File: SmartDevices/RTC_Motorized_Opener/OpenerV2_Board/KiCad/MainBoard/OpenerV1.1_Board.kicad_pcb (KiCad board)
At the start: 2 copper layers, 66 x 60 mm, 60 parts, among them IC1 CD4011BM96, J1 Motor, J2 Conn_01x02, J3 Conn_02x03_Odd_Even, J8 Conn_01x06, Q1 NPN, Q2 2N3904, Q3 AO3401A, Q4 AO3400A, Q5 2N3904, Q6 AO3400A, Q7 AO3401A, Q8 AO3400A, Q9 2N3904, SW1 Reset, SW2 Open, SW3 Menu, SW4 Close, U1 ATmega328P-AU, U2 MIC5205-5.0YM5, U3 DS1307, Y1 8/16MHz, Y2 32.768KHz

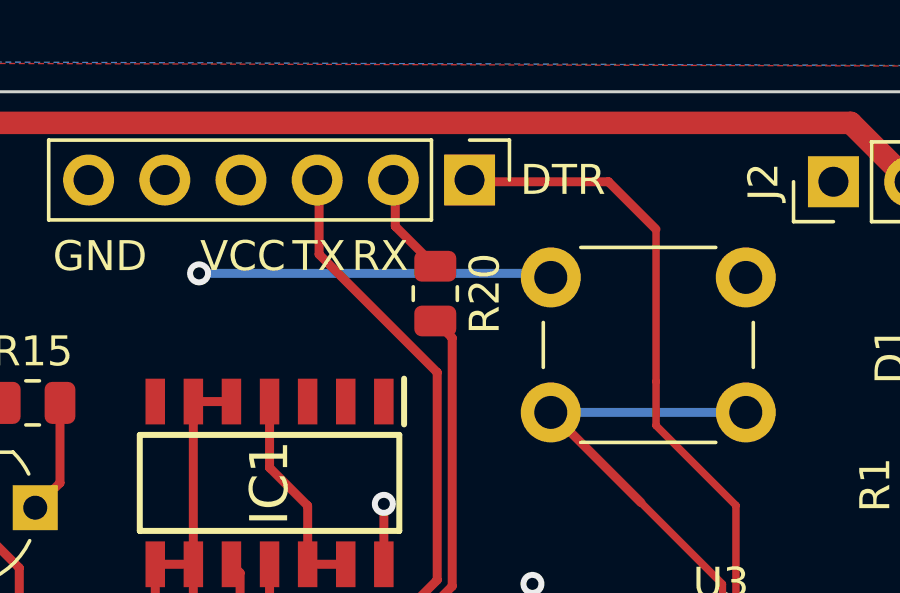
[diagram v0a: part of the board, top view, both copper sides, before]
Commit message: Fixed TX RX Swapped pins
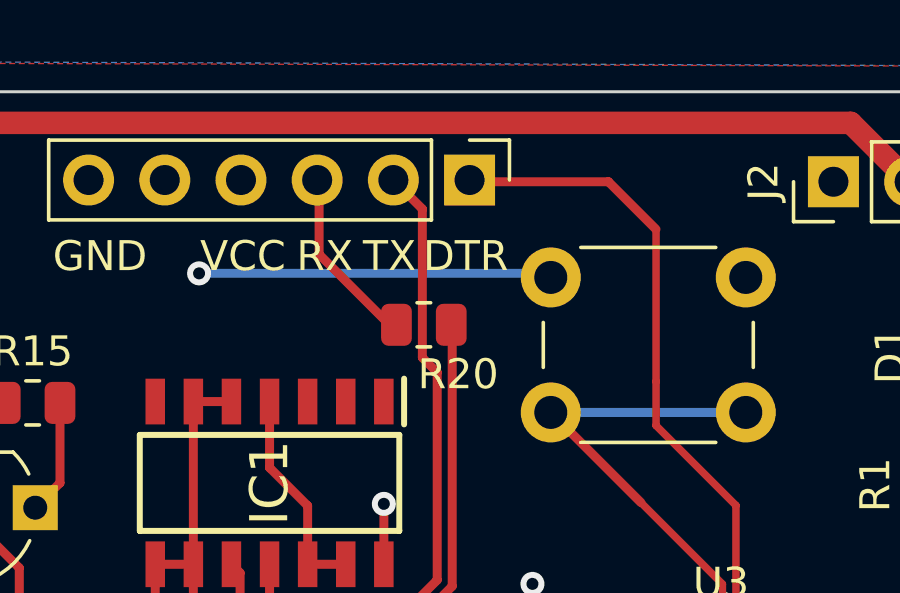
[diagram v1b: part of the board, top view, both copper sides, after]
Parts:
- moved R20 1.11 mm to (130.8, 48.8), turned to 0 degrees
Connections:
- J8 pad 2: Net-(J8-Pad2) -> Tx0
- J8 pad 3: Tx0 -> Net-(J8-Pad3)
- R20 pad 1: Net-(J8-Pad2) -> Net-(J8-Pad3)
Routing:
- net Net-(J8-Pad3): track 0.00 -> 5.97 mm
- net Net-(J8-Pad2): track 3.37 -> 0.00 mm
- net Tx0: track 38.6 -> 37.6 mm
- net Rx0: track 32.7 -> 31.9 mm

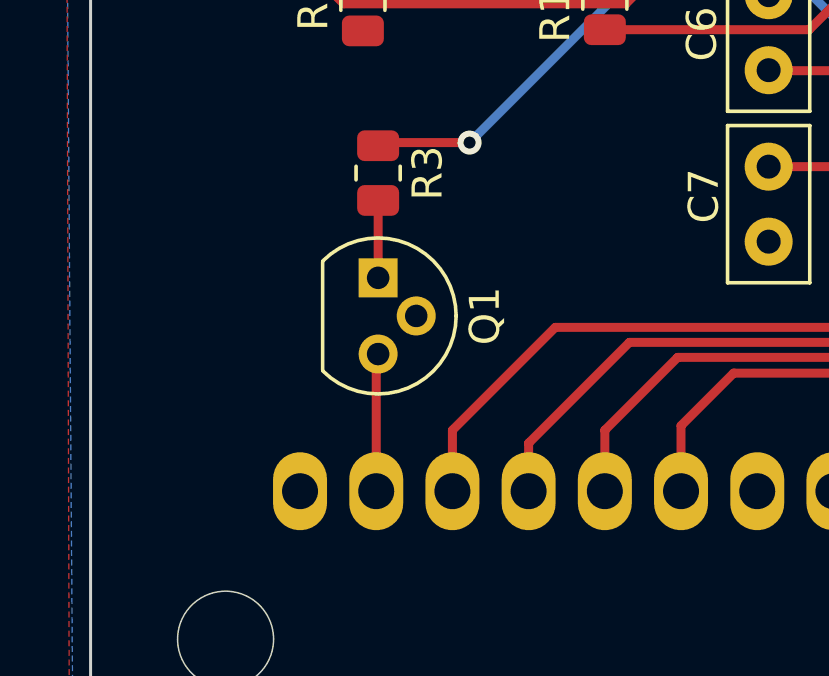
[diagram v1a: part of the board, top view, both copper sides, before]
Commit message: Fixed Transistor Orientation
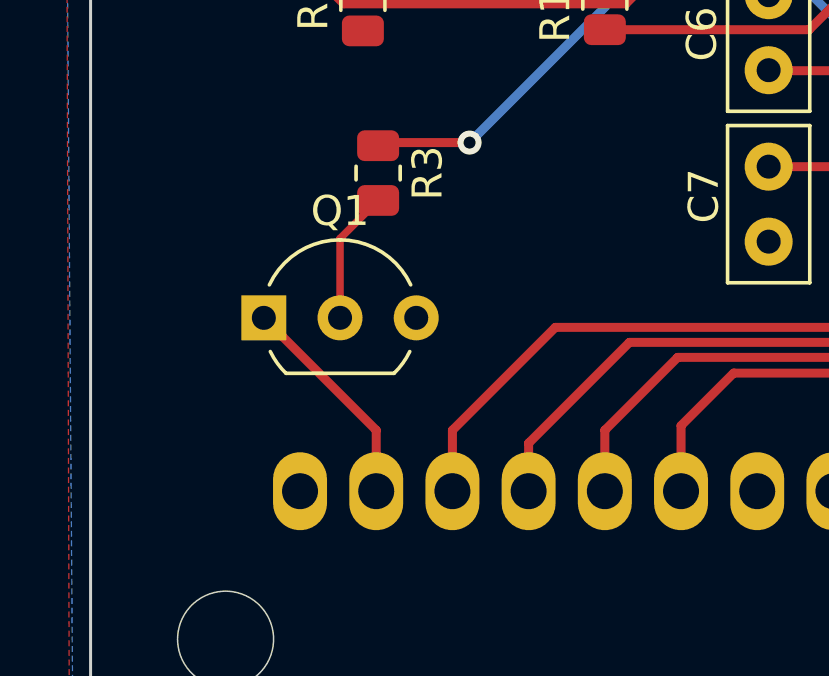
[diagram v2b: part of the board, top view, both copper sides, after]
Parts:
- Q1: value NPN -> 2N3904; footprint Package_TO_SOT_THT:TO-92 -> Package_TO_SOT_THT:TO-92_Inline_Wide
- moved Q1 4.04 mm to (104.8, 85.8), turned to 0 degrees
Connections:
- Q1 pad 1: Net-(Q1-Pad1) -> Net-(DS1-Pad15)
- Q1 pad 2: VCC -> Net-(Q1-Pad2)
- Q1 pad 3: Net-(DS1-Pad15) -> VCC
- R3 pad 2: Net-(Q1-Pad1) -> Net-(Q1-Pad2)
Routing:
- net Net-(Q1-Pad2): track 0.00 -> 4.44 mm
- net Net-(DS1-Pad15): track 4.60 -> 7.33 mm
- net Net-(Q1-Pad1): track 2.58 -> 0.00 mm
